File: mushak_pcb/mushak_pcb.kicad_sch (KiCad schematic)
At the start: 69 parts, among them J1 Conn_01x04_Male, J2 Conn_01x02_Female, J3 BLE_Conn, Q1 PN2222, SW1 SW_Push, SW2 SW_Push, U1 STM32F407VGTx, U2 TLV1117LV30DCYT, Y1 25Mhz, Y2 Crystal

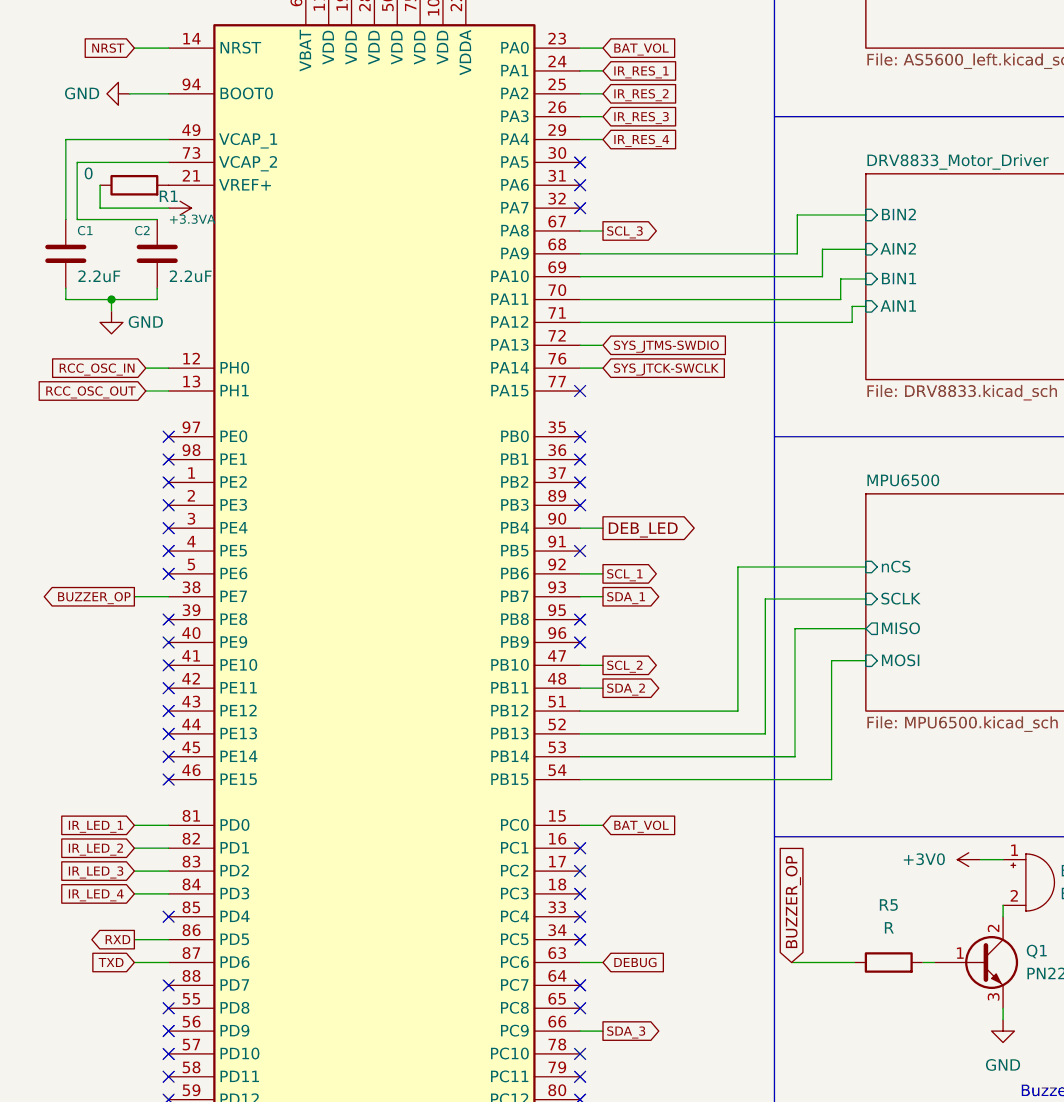
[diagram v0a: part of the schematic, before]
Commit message: Add footprints
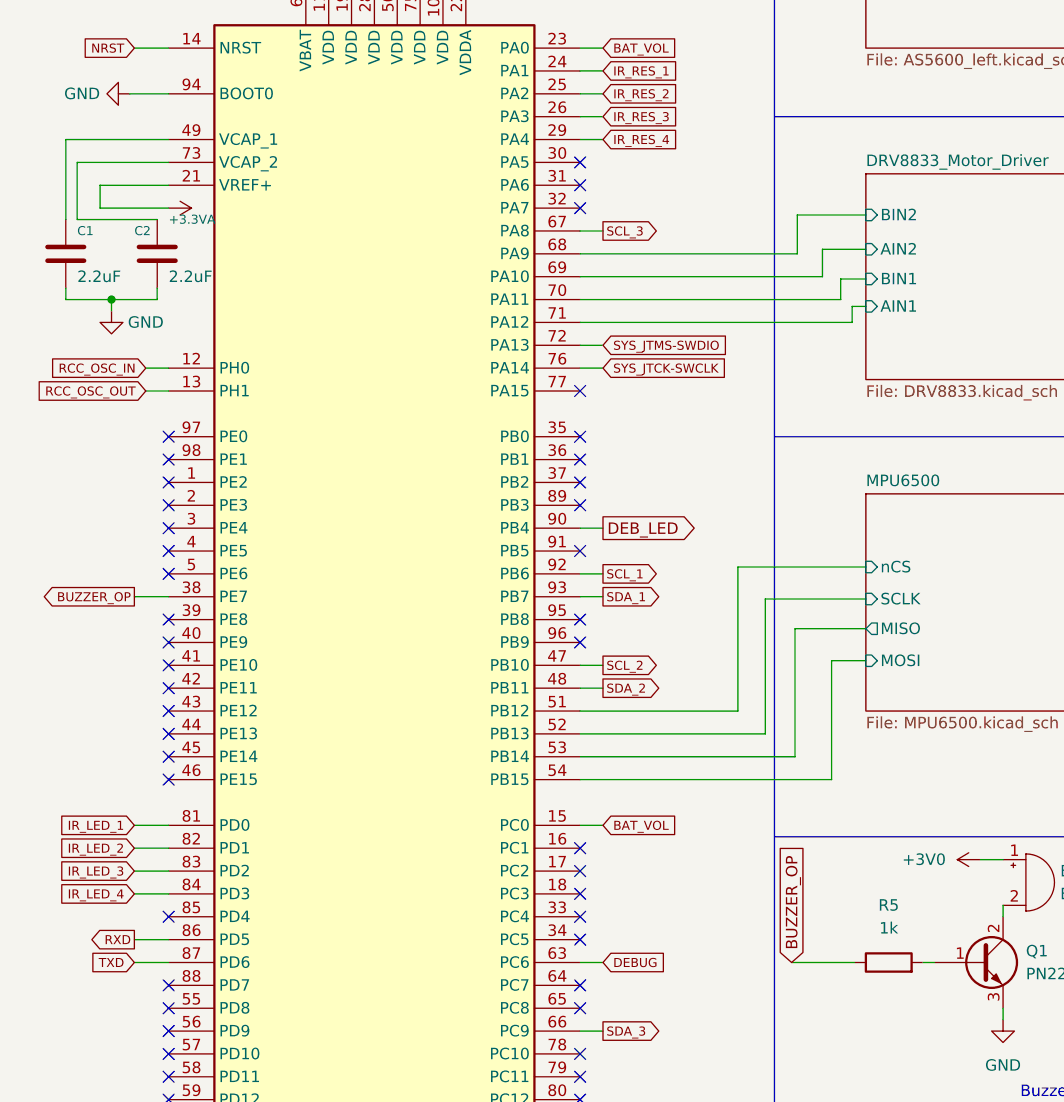
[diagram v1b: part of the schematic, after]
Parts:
- removed R1: 0, symbol Device:R
- BZ1: footprint (none) -> SMT-0440-T-R:XDCR_SMT-0440-T-R
- C1, C10, C11, C12, C13, C14, C15, C16, C17, C18, C19, C2, C20, C21, C3, C4, C5, C6, C7, C8, C9: footprint (none) -> Capacitor_SMD:C_0805_2012Metric
- D1, D6: footprint (none) -> LED_SMD:LED_0805_2012Metric
- FB1: footprint (none) -> Inductor_SMD:L_0805_2012Metric
- H1, H10, H11, H12, H13, H14, H2, H3, H4, H5, H6, H7, H8, H9: footprint (none) -> MountingHole:MountingHole_2.7mm_M2.5_Pad_Via
- J1, J3: footprint (none) -> Connector_PinHeader_2.54mm:PinHeader_1x04_P2.54mm_Vertical
- J2: footprint (none) -> Connector_JST:JST_EH_B2B-EH-A_1x02_P2.50mm_Vertical
- Q1: footprint (none) -> Package_TO_SOT_SMD:SOT-23
- R2, R21, R3, R4: footprint (none) -> Resistor_SMD:R_0805_2012Metric
- R5: value R -> 1k; footprint (none) -> Resistor_SMD:R_0805_2012Metric
- SW1, SW2: footprint (none) -> Button_Switch_SMD:SW_SPST_CK_RS282G05A3
- Y1: footprint (none) -> Crystal:Crystal_SMD_3225-4Pin_3.2x2.5mm
- Y2: footprint (none) -> Crystal:Crystal_C38-LF_D3.0mm_L8.0mm_Horizontal
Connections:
- net +3.3VA: now also U1.21 (VREF+)

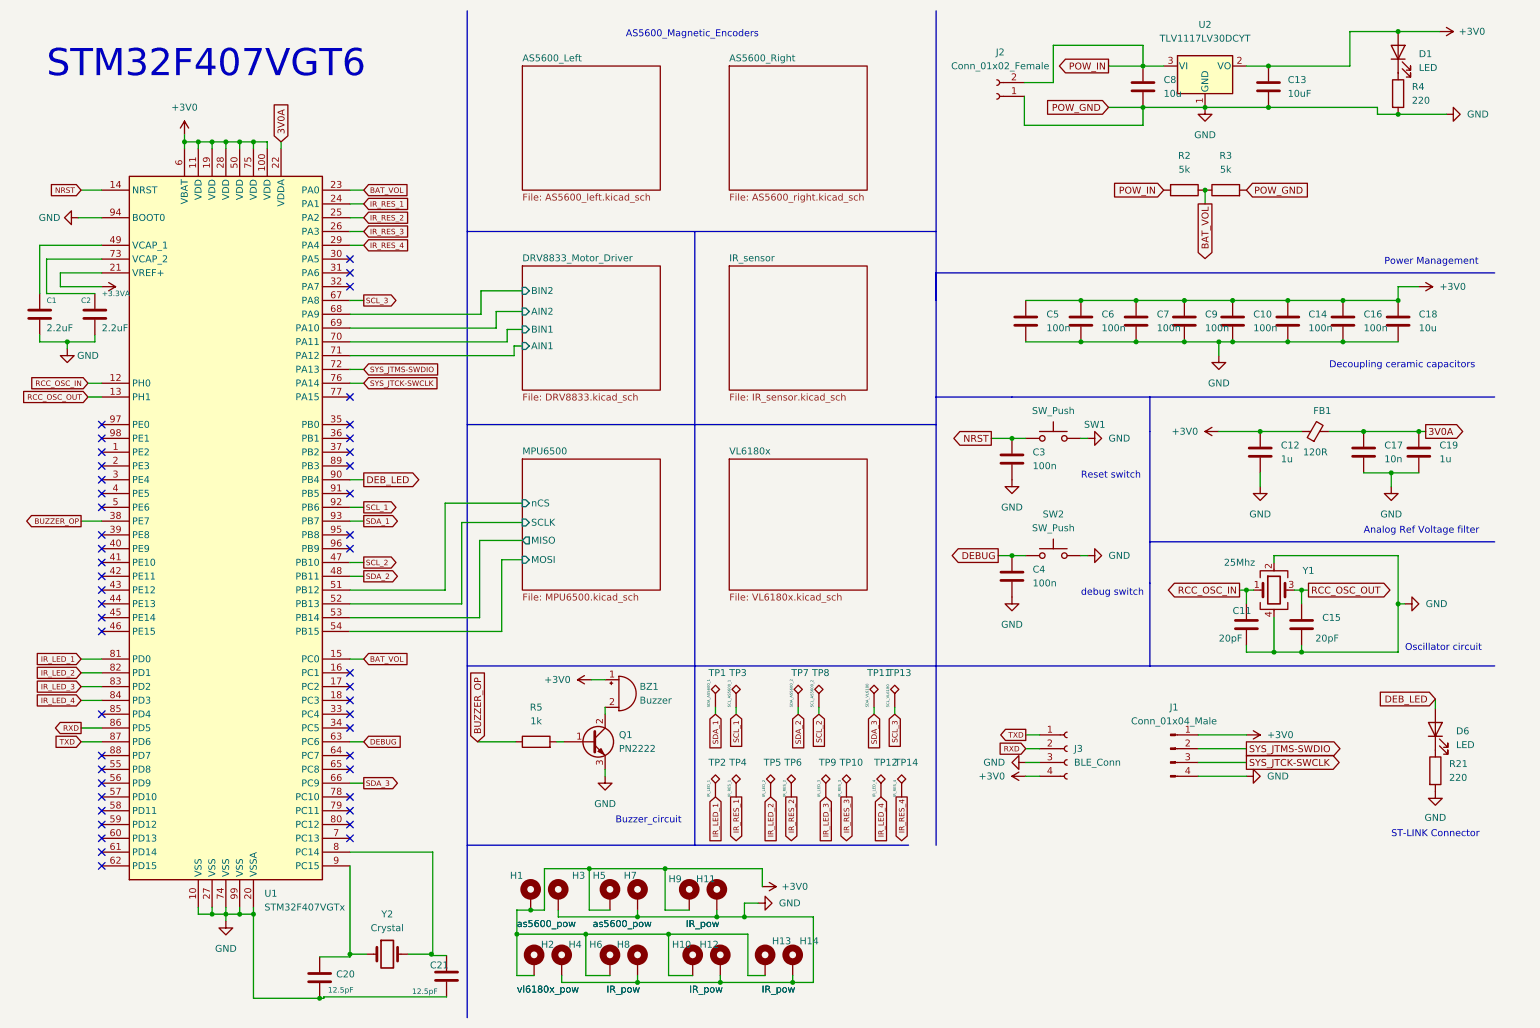
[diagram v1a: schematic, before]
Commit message: Update Schematics and footprints for sensors
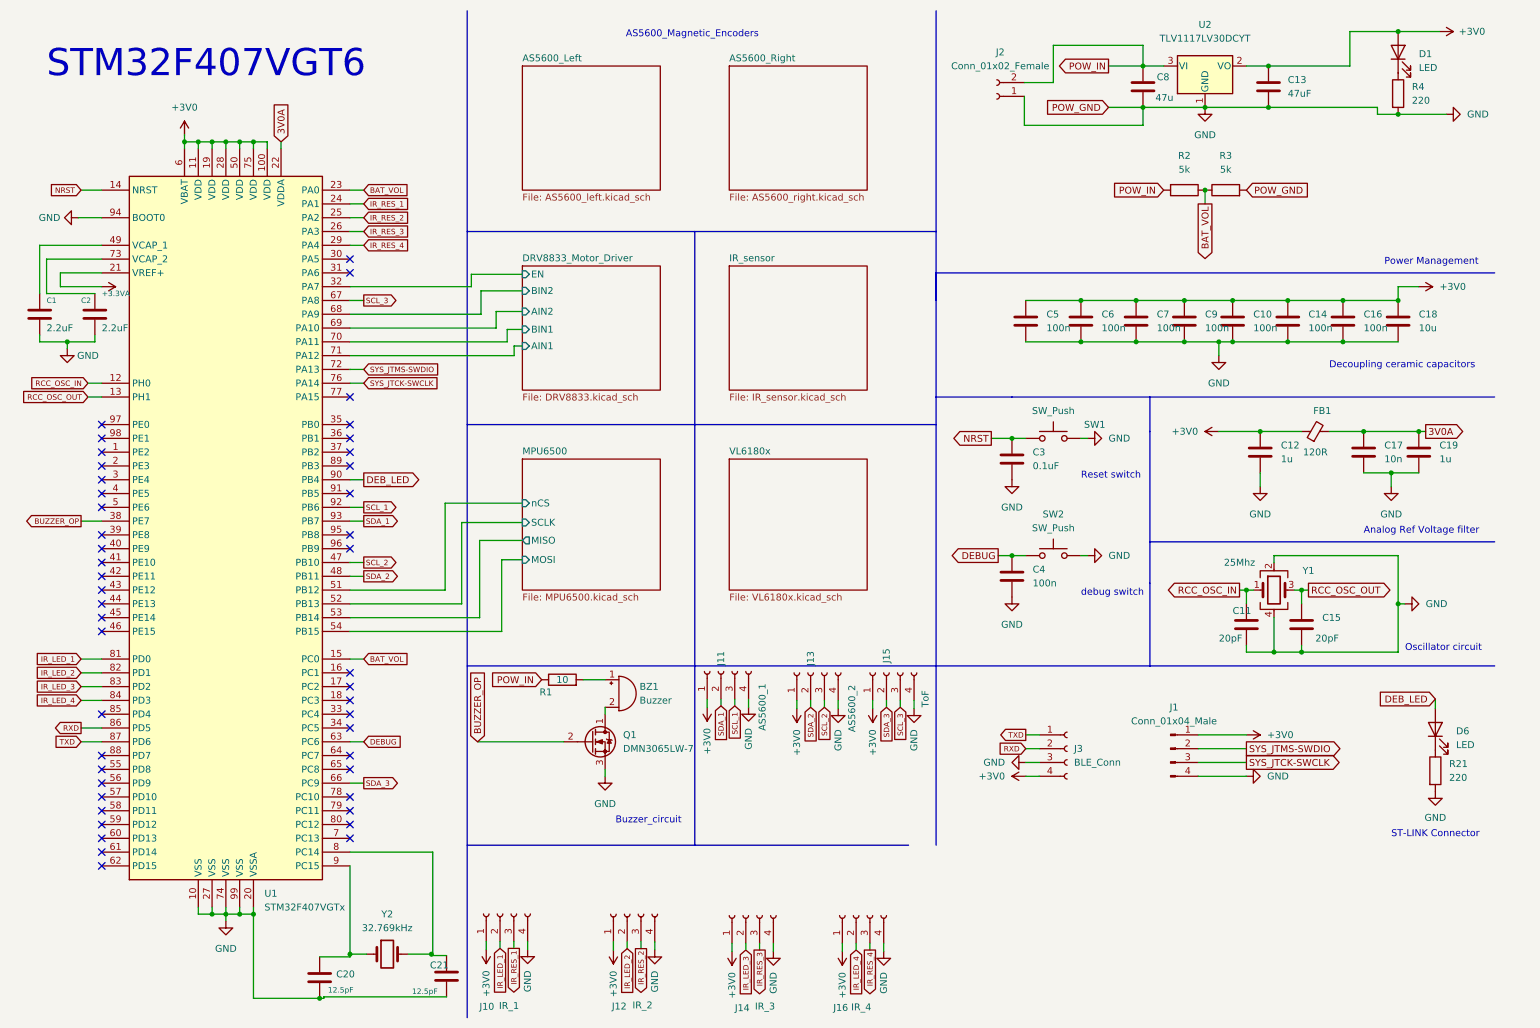
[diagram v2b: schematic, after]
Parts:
- removed H1, H3, H5, H7: as5600_pow, MountingHole:MountingHole_2.7mm_M2.5_Pad_Via, symbol Mechanical:MountingHole_Pad
- removed H10, H11, H12, H13, H14, H6, H8, H9: IR_pow, MountingHole:MountingHole_2.7mm_M2.5_Pad_Via, symbol Mechanical:MountingHole_Pad
- removed H2, H4: vl6180x_pow, MountingHole:MountingHole_2.7mm_M2.5_Pad_Via, symbol Mechanical:MountingHole_Pad
- removed Q1: PN2222, Package_TO_SOT_SMD:SOT-23, symbol Device:Q_NPN_BCE
- removed R5: 1k, Resistor_SMD:R_0805_2012Metric, symbol Device:R
- removed TP1: SDA_AS5600_1, TestPoint:TestPoint_Keystone_5019_Minature, symbol Connector:TestPoint_Alt
- removed TP10: IR_RES_3, TestPoint:TestPoint_Keystone_5019_Minature, symbol Connector:TestPoint_Alt
- removed TP11: SDA_VL6180, TestPoint:TestPoint_Keystone_5019_Minature, symbol Connector:TestPoint_Alt
- removed TP12: IR_LED_4, TestPoint:TestPoint_Keystone_5019_Minature, symbol Connector:TestPoint_Alt
- removed TP13: SCL_VL6180, TestPoint:TestPoint_Keystone_5019_Minature, symbol Connector:TestPoint_Alt
- removed TP14: IR_RES_4, TestPoint:TestPoint_Keystone_5019_Minature, symbol Connector:TestPoint_Alt
- removed TP2: IR_LED_1, TestPoint:TestPoint_Keystone_5019_Minature, symbol Connector:TestPoint_Alt
- removed TP3: SCL_AS5600_1, TestPoint:TestPoint_Keystone_5019_Minature, symbol Connector:TestPoint_Alt
- removed TP4: IR_RES_1, TestPoint:TestPoint_Keystone_5019_Minature, symbol Connector:TestPoint_Alt
- removed TP5: IR_LED_2, TestPoint:TestPoint_Keystone_5019_Minature, symbol Connector:TestPoint_Alt
- removed TP6: IR_RES_2, TestPoint:TestPoint_Keystone_5019_Minature, symbol Connector:TestPoint_Alt
- removed TP7: SDA_AS5600_2, TestPoint:TestPoint_Keystone_5019_Minature, symbol Connector:TestPoint_Alt
- removed TP8: SCL_AS5600_2, TestPoint:TestPoint_Keystone_5019_Minature, symbol Connector:TestPoint_Alt
- removed TP9: IR_LED_3, TestPoint:TestPoint_Keystone_5019_Minature, symbol Connector:TestPoint_Alt
- added J10: IR_1, mushak_mount_footprint:IR_HOST_V_04, symbol Connector:Conn_01x04_Female
- added J11: AS5600_1, mushak_mount_footprint:STAND_HOST_04, symbol Connector:Conn_01x04_Female
- added J12: IR_2, mushak_mount_footprint:IR_HOST_V_04, symbol Connector:Conn_01x04_Female
- added J13: AS5600_2, mushak_mount_footprint:STAND_HOST_04, symbol Connector:Conn_01x04_Female
- added J14: IR_3, mushak_mount_footprint:IR_HOST_V_04, symbol Connector:Conn_01x04_Female
- added J15: ToF, mushak_mount_footprint:STAND_HOST_04, symbol Connector:Conn_01x04_Female
- added J16: IR_4, mushak_mount_footprint:IR_HOST_V_04, symbol Connector:Conn_01x04_Female
- added Q1: DMN3065LW-7, Package_TO_SOT_SMD:SOT-323_SC-70, symbol Device:Q_NMOS_DGS
- added R1: 10, Resistor_SMD:R_0402_1005Metric, symbol Device:R
- C1, C10, C11, C12, C14, C15, C16, C17, C18, C19, C2, C20, C21, C4, C5, C6, C7, C9: footprint Capacitor_SMD:C_0805_2012Metric -> Capacitor_SMD:C_0402_1005Metric
- C13: value 10uF -> 47uF; footprint Capacitor_SMD:C_0805_2012Metric -> Capacitor_SMD:C_0402_1005Metric
- C3: value 100n -> 0.1uF; footprint Capacitor_SMD:C_0805_2012Metric -> Capacitor_SMD:C_0402_1005Metric
- C8: value 10u -> 47u; footprint Capacitor_SMD:C_0805_2012Metric -> Capacitor_SMD:C_0402_1005Metric
- D1, D6: footprint LED_SMD:LED_0805_2012Metric -> LED_SMD:LED_0402_1005Metric
- J1: footprint Connector_PinHeader_2.54mm:PinHeader_1x04_P2.54mm_Vertical -> Connector_JST:JST_SH_SM04B-SRSS-TB_1x04-1MP_P1.00mm_Horizontal
- R2, R21, R3, R4: footprint Resistor_SMD:R_0805_2012Metric -> Resistor_SMD:R_0402_1005Metric
- Y2: value Crystal -> 32.769kHz; footprint Crystal:Crystal_C38-LF_D3.0mm_L8.0mm_Horizontal -> ABS07-32:XTAL_ABS07-32.768KHZ-T
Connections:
- net +3V0: now also J10.1 (Pin_1), J11.1 (Pin_1), J12.1 (Pin_1), J13.1 (Pin_1), J14.1 (Pin_1), J15.1 (Pin_1), J16.1 (Pin_1); no longer BZ1.1 (-)
- net BUZZER_OP: now also Q1.2 (G)
- net GND: now also J10.4 (Pin_4), J11.4 (Pin_4), J12.4 (Pin_4), J13.4 (Pin_4), J14.4 (Pin_4), J15.4 (Pin_4), J16.4 (Pin_4), Q1.3 (S)
- net IR_LED_1: now also J10.2 (Pin_2)
- net IR_LED_2: now also J12.2 (Pin_2)
- net IR_LED_3: now also J14.2 (Pin_2)
- net IR_LED_4: now also J16.2 (Pin_2)
- net IR_RES_1: now also J10.3 (Pin_3)
- net IR_RES_2: now also J12.3 (Pin_3)
- net IR_RES_3: now also J14.3 (Pin_3)
- net IR_RES_4: now also J16.3 (Pin_3)
- net POW_IN: now also R1.1
- net SCL_1: now also J11.3 (Pin_3)
- net SCL_2: now also J13.3 (Pin_3)
- net SCL_3: now also J15.3 (Pin_3)
- net SDA_1: now also J11.2 (Pin_2)
- net SDA_2: now also J13.2 (Pin_2)
- net SDA_3: now also J15.2 (Pin_2)
- net at BZ1.2 (+): now also Q1.1 (D)
- net DRV8833_Motor_Driver/EN: now reaches U1.32 (PA7)
- new net: BZ1.1 (-), R1.2
- no-connect marks 47 -> 46
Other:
- sheet DRV8833_Motor_Driver ports: added EN; removed none
